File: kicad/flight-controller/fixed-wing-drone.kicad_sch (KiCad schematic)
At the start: 0 parts

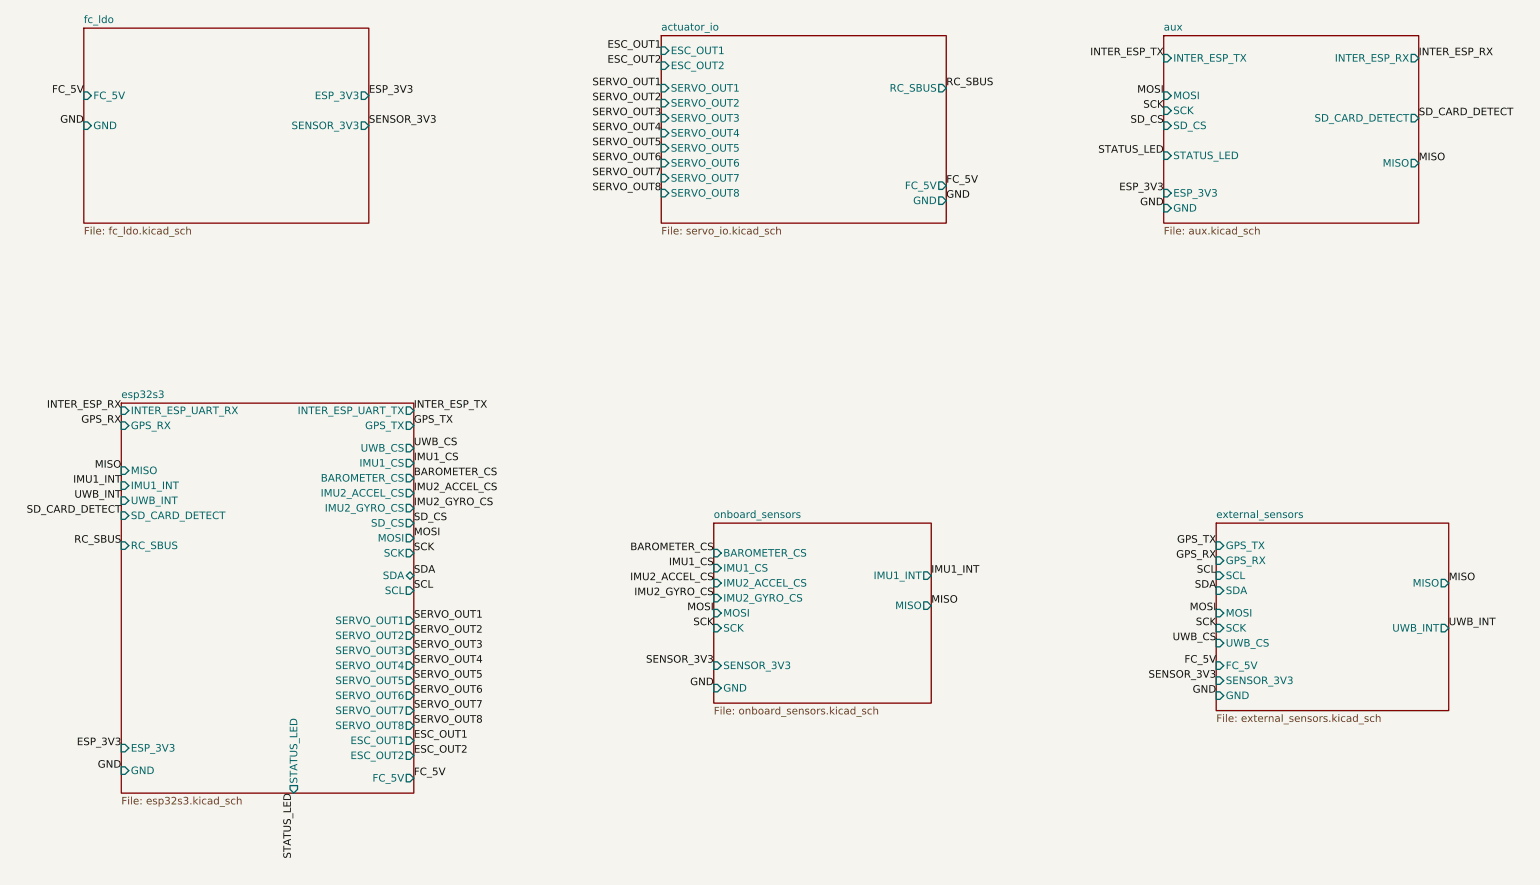
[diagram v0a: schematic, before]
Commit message: removed basestation code and v3.1 of fc pcb
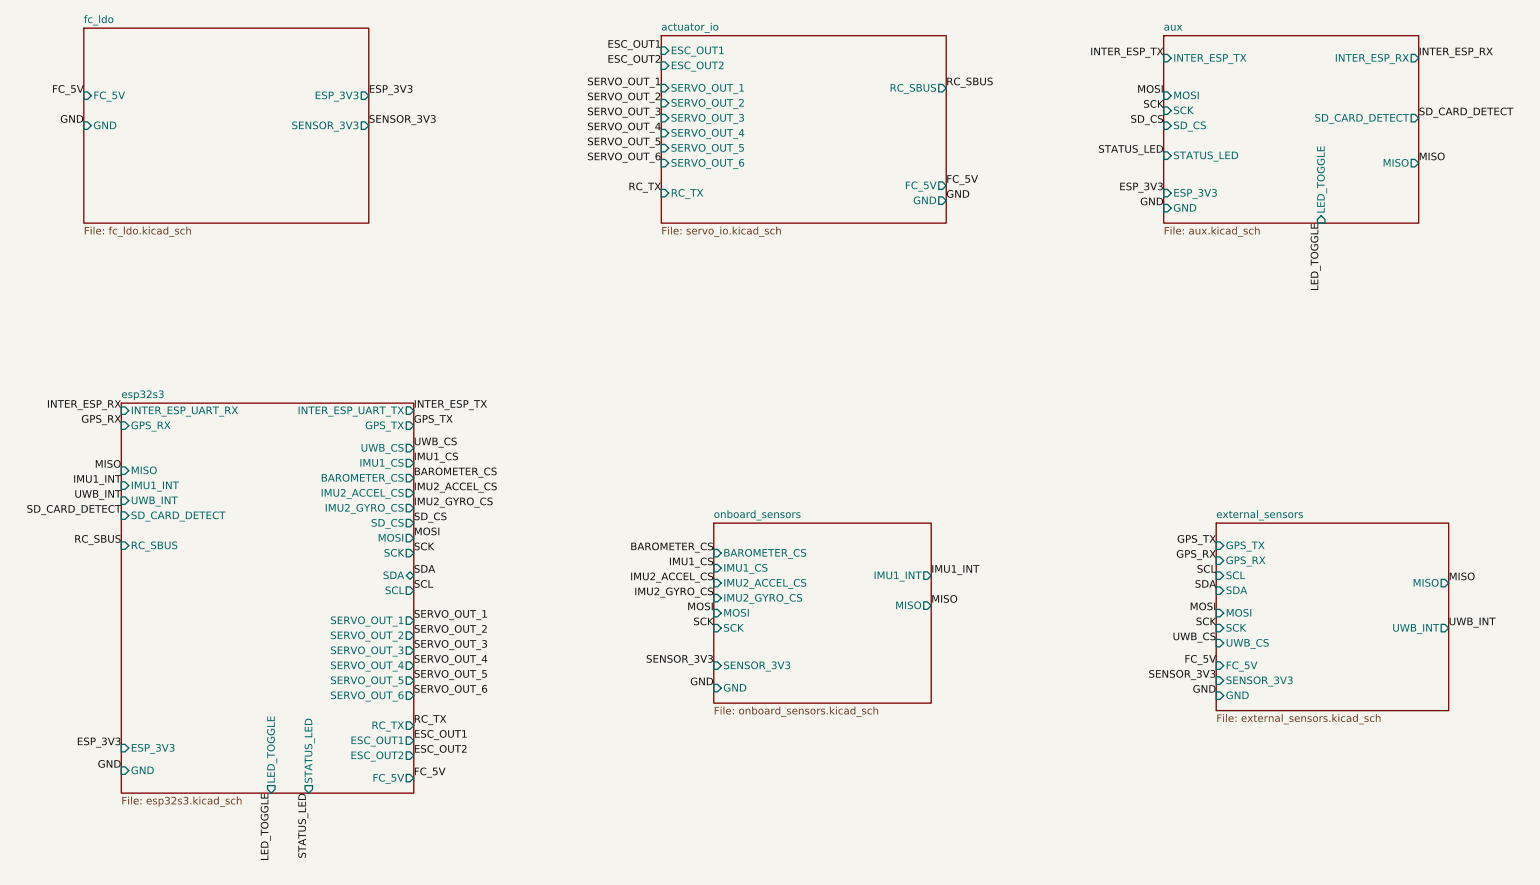
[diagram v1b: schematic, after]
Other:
- sheet actuator_io ports: added RC_TX, SERVO_OUT_1, SERVO_OUT_2, SERVO_OUT_3, SERVO_OUT_4, SERVO_OUT_5, SERVO_OUT_6; removed SERVO_OUT1, SERVO_OUT2, SERVO_OUT3, SERVO_OUT4, SERVO_OUT5, SERVO_OUT6, SERVO_OUT7, SERVO_OUT8
- sheet aux ports: added LED_TOGGLE; removed none
- sheet esp32s3 ports: added LED_TOGGLE, RC_TX, SERVO_OUT_1, SERVO_OUT_2, SERVO_OUT_3, SERVO_OUT_4, SERVO_OUT_5, SERVO_OUT_6; removed SERVO_OUT1, SERVO_OUT2, SERVO_OUT3, SERVO_OUT4, SERVO_OUT5, SERVO_OUT6, SERVO_OUT7, SERVO_OUT8
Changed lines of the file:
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@@
 		)
 	)
-	(label "SERVO_OUT6"
+	(label "SERVO_OUT_6"
 		(at 127 48.26 180)
 		(effects
@@
 		)
 	)
-	(label "SERVO_OUT1"
+	(label "LED_TOGGLE"
+		(at 60.96 154.94 270)
+		(effects
+			(font
+				(size 1.27 1.27)
+			)
+			(justify right bottom)
+		)
+	)
+	(label "SERVO_OUT_1"
 		(at 85.09 125.73 0)
 		(effects
@@
 		)
 	)
-	(label "SERVO_OUT3"
+	(label "SERVO_OUT_3"
 		(at 127 40.64 180)
 		(effects
@@
 		)
 	)
-	(label "SERVO_OUT7"
-		(at 85.09 140.97 0)
-		(effects
-			(font
-				(size 1.27 1.27)
-			)
-			(justify left bottom)
-		)
-	)
-	(label "SERVO_OUT8"
+	(label "RC_TX"
 		(at 127 53.34 180)
 		(effects
@@
 		)
 	)
-	(label "SERVO_OUT8"
+	(label "RC_TX"
 		(at 85.09 143.51 0)
 		(effects
@@
 		)
 	)
+	(label "LED_TOGGLE"
+		(at 238.76 58.42 270)
+		(effects
+			(font
+				(size 1.27 1.27)
+			)
+			(justify right bottom)
+		)
+	)
 	(label "MOSI"
 		(at 212.09 36.83 180)
@@
 		)
 	)
-	(label "SERVO_OUT3"
+	(label "SERVO_OUT_3"
 		(at 85.09 130.81 0)
 		(effects
@@
 		)
 	)
-	(label "SERVO_OUT7"
-		(at 127 50.8 180)
-		(effects
-			(font
-				(size 1.27 1.27)
-			)
-			(justify right bottom)
-		)
-	)
 	(label "STATUS_LED"
-		(at 64.77 154.94 270)
+		(at 67.31 154.94 270)
 		(effects
 			(font
@@
 		)
 	)
-	(label "SERVO_OUT1"
+	(label "SERVO_OUT_1"
 		(at 127 35.56 180)
 		(effects
@@
 		)
 	)
-	(label "SERVO_OUT5"
+	(label "SERVO_OUT_5"
 		(at 127 45.72 180)
 		(effects
@@
 		)
 	)
-	(label "SERVO_OUT4"
+	(label "SERVO_OUT_4"
 		(at 85.09 133.35 0)
 		(effects
@@
 		)
 	)
-	(label "SERVO_OUT2"
+	(label "SERVO_OUT_2"
 		(at 85.09 128.27 0)
 		(effects
@@
 		)
 	)
-	(label "SERVO_OUT2"
+	(label "SERVO_OUT_2"
 		(at 127 38.1 180)
 		(effects
@@
 		)
 	)
-	(label "SERVO_OUT6"
+	(label "SERVO_OUT_6"
 		(at 85.09 138.43 0)
 		(effects
@@
 		)
 	)
-	(label "SERVO_OUT4"
+	(label "SERVO_OUT_4"
 		(at 127 43.18 180)
 		(effects
@@
 		)
 	)
-	(label "SERVO_OUT5"
+	(label "SERVO_OUT_5"
 		(at 85.09 135.89 0)
 		(effects
@@
 			)
 		)
+		(pin "LED_TOGGLE" input
+			(at 238.76 58.42 270)
+			(effects
+				(font
+					(size 1.27 1.27)
+				)
+				(justify left)
+			)
+		)
 		(instances
 			(project "fixed-wing-drone"
@@
 			)
 		)
-		(pin "SERVO_OUT1" input
+		(pin "SERVO_OUT_1" input
 			(at 127 35.56 180)
 			(effects
@@
 			)
 		)
-		(pin "SERVO_OUT2" input
+		(pin "SERVO_OUT_2" input
 			(at 127 38.1 180)
 			(effects
@@
 			)
 		)
-		(pin "SERVO_OUT3" input
+		(pin "SERVO_OUT_3" input
 			(at 127 40.64 180)
 			(effects
@@
 			)
 		)
-		(pin "SERVO_OUT4" input
+		(pin "SERVO_OUT_4" input
 			(at 127 43.18 180)
 			(effects
@@
 			)
 		)
-		(pin "SERVO_OUT5" input
+		(pin "SERVO_OUT_5" input
 			(at 127 45.72 180)
 			(effects
@@
 			)
 		)
-		(pin "SERVO_OUT6" input
+		(pin "SERVO_OUT_6" input
 			(at 127 48.26 180)
 			(effects
@@
 			)
 		)
-		(pin "SERVO_OUT7" input
-			(at 127 50.8 180)
-			(effects
-				(font
-					(size 1.27 1.27)
-				)
-				(justify left)
-			)
-		)
-		(pin "SERVO_OUT8" input
+		(pin "RC_TX" input
 			(at 127 53.34 180)
 			(effects
@@
 			)
 		)
-		(pin "SERVO_OUT1" output
+		(pin "SERVO_OUT_1" output
 			(at 85.09 125.73 0)
 			(effects
@@
 			)
 		)
-		(pin "SERVO_OUT2" output
+		(pin "SERVO_OUT_2" output
 			(at 85.09 128.27 0)
 			(effects
@@
 			)
 		)
-		(pin "SERVO_OUT3" output
+		(pin "SERVO_OUT_3" output
 			(at 85.09 130.81 0)
 			(effects
@@
 			)
 		)
-		(pin "SERVO_OUT4" output
+		(pin "SERVO_OUT_4" output
 			(at 85.09 133.35 0)
 			(effects
@@
 			)
 		)
-		(pin "SERVO_OUT5" output
+		(pin "SERVO_OUT_5" output
 			(at 85.09 135.89 0)
 			(effects
@@
 			)
 		)
-		(pin "SERVO_OUT6" output
+		(pin "SERVO_OUT_6" output
 			(at 85.09 138.43 0)
 			(effects
@@
 			)
 		)
-		(pin "SERVO_OUT7" output
-			(at 85.09 140.97 0)
-			(effects
-				(font
-					(size 1.27 1.27)
-				)
-				(justify right)
-			)
-		)
-		(pin "SERVO_OUT8" output
+		(pin "RC_TX" output
 			(at 85.09 143.51 0)
 			(effects
@@
 		)
 		(pin "STATUS_LED" output
-			(at 64.77 154.94 270)
+			(at 67.31 154.94 270)
 			(effects
 				(font
@@
 			(effects
 				(font
+					(size 1.27 1.27)
+				)
+				(justify left)
+			)
+		)
+		(pin "LED_TOGGLE" output
+			(at 60.96 154.94 270)
+			(effects
+				(font

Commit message: Kicad FC v3.1 complete, Mission Controller and UWB boards v1 complete, firmware v2 complete!
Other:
- sheet aux ports: added SD_MISO, SD_MOSI, SD_SCK; removed MISO, MOSI, SCK
- sheet esp32s3 ports: added SD_MISO, SD_MOSI, SD_SCK; removed none
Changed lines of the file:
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@@
 		)
 	)
-	(label "MOSI"
+	(label "SD_MOSI"
 		(at 212.09 36.83 180)
 		(effects
@@
 		)
 	)
-	(label "MISO"
+	(label "SD_MISO"
 		(at 255.27 48.26 0)
 		(effects
@@
 		)
 	)
+	(label "SD_MISO"
+		(at 35.56 118.11 180)
+		(effects
+			(font
+				(size 1.27 1.27)
+			)
+			(justify right bottom)
+		)
+	)
 	(label "SCK"
 		(at 220.98 127 180)
@@
 		)
 	)
+	(label "SD_MOSI"
+		(at 35.56 120.65 180)
+		(effects
+			(font
+				(size 1.27 1.27)
+			)
+			(justify right bottom)
+		)
+	)
 	(label "RC_SBUS"
 		(at 175.26 35.56 0)
@@
 		)
 	)
-	(label "SCK"
+	(label "SD_SCK"
 		(at 212.09 39.37 180)
 		(effects
@@
 	(label "FC_5V"
 		(at 29.21 36.83 180)
+		(effects
+			(font
+				(size 1.27 1.27)
+			)
+			(justify right bottom)
+		)
+	)
+	(label "SD_SCK"
+		(at 35.56 123.19 180)
 		(effects
 			(font
@@
 			)
 		)
-		(pin "MISO" output
+		(pin "SD_MISO" output
 			(at 255.27 48.26 0)
 			(effects
@@
 			)
 		)
-		(pin "MOSI" input
+		(pin "SD_MOSI" input
 			(at 212.09 36.83 180)
 			(effects
@@
 			)
 		)
-		(pin "SCK" input
+		(pin "SD_SCK" input
 			(at 212.09 39.37 180)
 			(effects
@@
 			)
 		)
+		(pin "SD_MISO" input
+			(at 35.56 118.11 180)
+			(effects
+				(font
+					(size 1.27 1.27)
+				)
+				(justify left)
+			)
+		)
+		(pin "SD_MOSI" output
+			(at 35.56 120.65 180)
+			(effects
+				(font
+					(size 1.27 1.27)
+				)
+				(justify left)
+			)
+		)
+		(pin "SD_SCK" output
+			(at 35.56 123.19 180)
+			(effects
+				(font
+					(size 1.27 1.27)
+				)
+				(justify left)
+			)
+		)
